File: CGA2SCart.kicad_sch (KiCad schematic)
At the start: 34 parts, among them J1 SCART-F, J2 DB9_Male, J3 Audio-Jack-3_2Switches, J4 DB15_Female_HighDensity, Q1 2N7000

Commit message: Other connections fixed
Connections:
- net at J1.11 (P11), R16.2, R7.2: now also JP3.2 (B), JP7.2 (B)
- net at J1.7 (P7), R17.2, R6.2: now also JP2.2 (B), JP5.2 (B)
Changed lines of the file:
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@@
   (junction (at 221.615 96.52) (diameter 0) (color 0 0 0 0)
   )
+  (junction (at 151.13 97.79) (diameter 0) (color 0 0 0 0)
+  )
   (junction (at 142.875 102.87) (diameter 0) (color 0 0 0 0)
   )
@@
   (junction (at 165.735 87.63) (diameter 0) (color 0 0 0 0)
   )
+  (junction (at 156.845 87.63) (diameter 0) (color 0 0 0 0)
+  )
   (junction (at 151.13 131.445) (diameter 0) (color 0 0 0 0)
   )
@@
     (stroke (width 0) (type default) (color 0 0 0 0))
   )
+  (wire (pts (xy 156.845 87.63) (xy 165.735 87.63))
+    (stroke (width 0) (type default) (color 0 0 0 0))
+  )
   (wire (pts (xy 156.845 131.445) (xy 162.56 131.445))
     (stroke (width 0) (type default) (color 0 0 0 0))
@@
     (stroke (width 0) (type default) (color 0 0 0 0))
   )
-  (wire (pts (xy 156.845 74.295) (xy 156.845 102.235))
+  (wire (pts (xy 151.13 97.79) (xy 165.735 97.79))
     (stroke (width 0) (type default) (color 0 0 0 0))
   )
@@
     (stroke (width 0) (type default) (color 0 0 0 0))
   )
-  (wire (pts (xy 140.97 87.63) (xy 165.735 87.63))
+  (wire (pts (xy 140.97 87.63) (xy 156.845 87.63))
     (stroke (width 0) (type default) (color 0 0 0 0))
   )
@@
     (stroke (width 0) (type default) (color 0 0 0 0))
   )
+  (wire (pts (xy 156.845 87.63) (xy 156.845 102.235))
+    (stroke (width 0) (type default) (color 0 0 0 0))
+  )
   (wire (pts (xy 221.615 135.89) (xy 224.155 135.89))
     (stroke (width 0) (type default) (color 0 0 0 0))
   )
-  (wire (pts (xy 140.97 97.79) (xy 165.735 97.79))
+  (wire (pts (xy 140.97 97.79) (xy 151.13 97.79))
     (stroke (width 0) (type default) (color 0 0 0 0))
   )
@@
     (stroke (width 0) (type default) (color 0 0 0 0))
   )
+  (wire (pts (xy 156.845 74.295) (xy 156.845 87.63))
+    (stroke (width 0) (type default) (color 0 0 0 0))
+  )
   (wire (pts (xy 95.25 104.775) (xy 99.695 104.775))
     (stroke (width 0) (type default) (color 0 0 0 0))
@@
     (stroke (width 0) (type default) (color 0 0 0 0))
   )
+  (wire (pts (xy 151.13 97.79) (xy 151.13 102.235))
+    (stroke (width 0) (type default) (color 0 0 0 0))
+  )
+  (wire (pts (xy 151.13 74.295) (xy 151.13 97.79))
+    (stroke (width 0) (type default) (color 0 0 0 0))
+  )
   (wire (pts (xy 162.56 130.175) (xy 162.56 131.445))
     (stroke (width 0) (type default) (color 0 0 0 0))
@@
     (stroke (width 0) (type default) (color 0 0 0 0))
   )
-  (wire (pts (xy 151.13 74.295) (xy 151.13 102.235))
-    (stroke (width 0) (type default) (color 0 0 0 0))
-  )

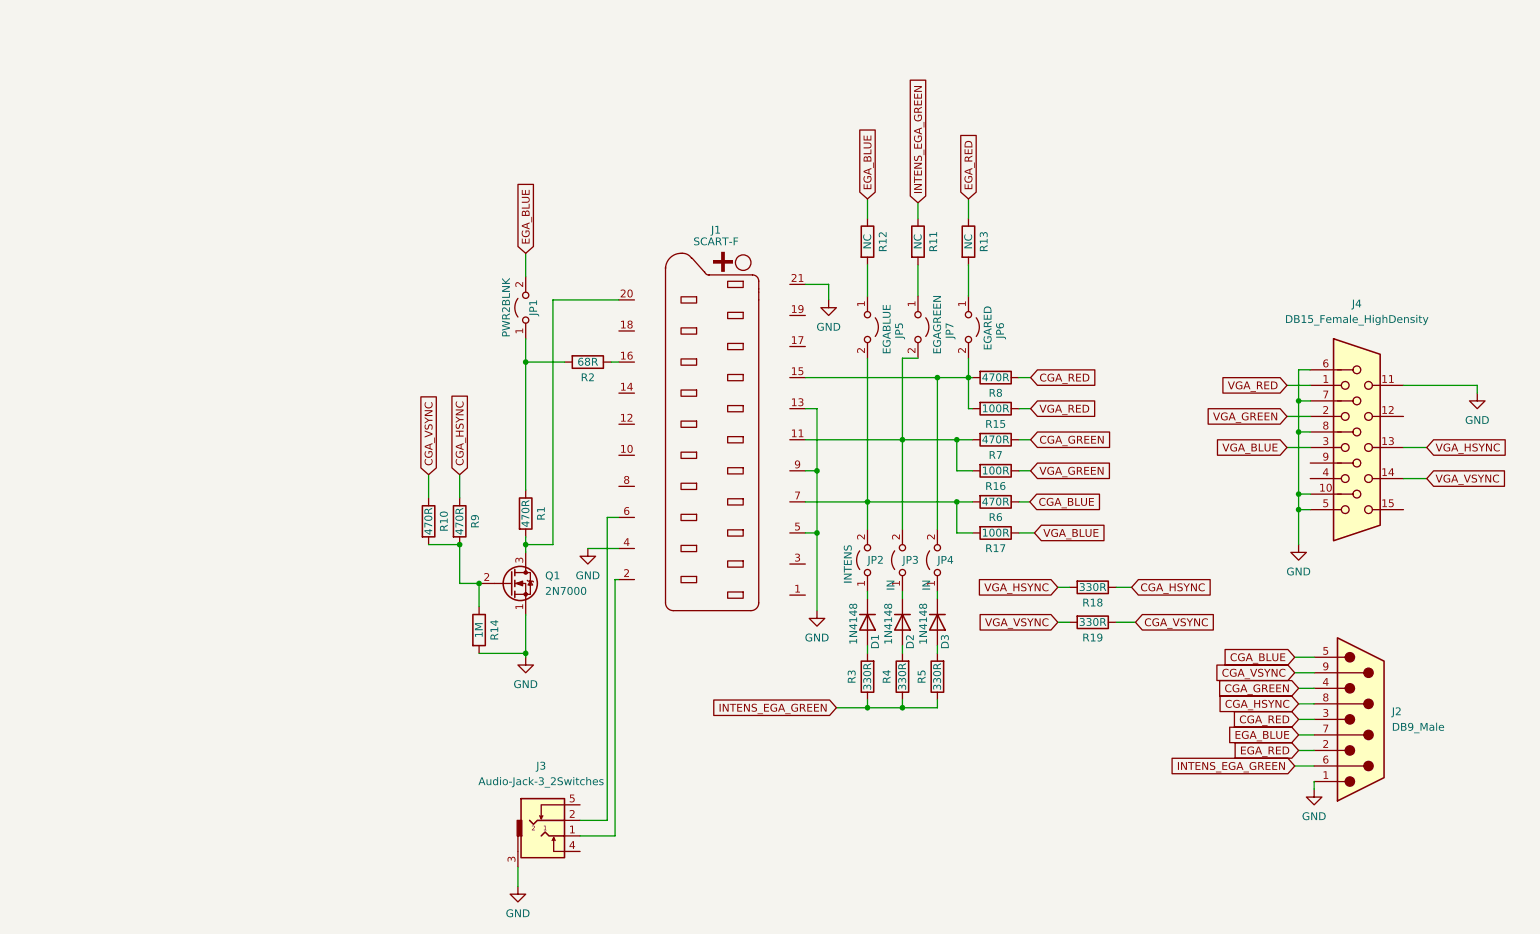
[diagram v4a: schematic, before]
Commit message: V3 of CGA2SCART, change CSYNC to XOR presync
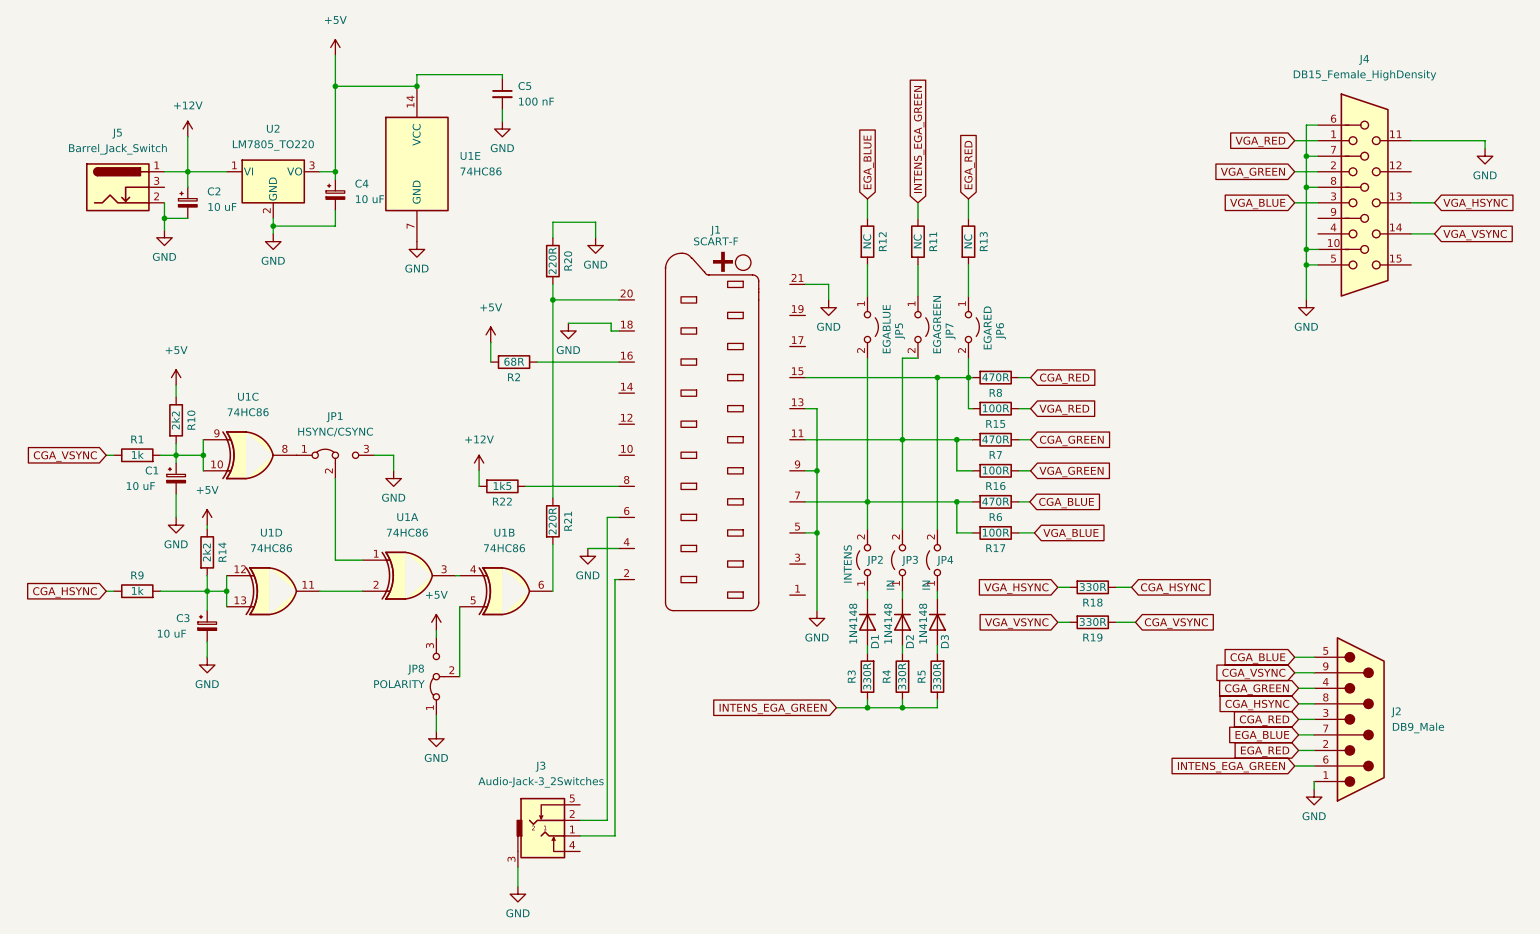
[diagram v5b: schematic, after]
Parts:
- removed JP1: PWR2BLNK, Connector_PinHeader_2.54mm:PinHeader_1x02_P2.54mm_Vertical, symbol Jumper:Jumper_2_Open
- removed Q1: 2N7000, Package_TO_SOT_THT:TO-92_Inline_Wide, symbol Transistor_FET:2N7000
- added C1, C2, C3, C4: 10 uF, Capacitor_THT:CP_Radial_D5.0mm_P2.00mm, symbol Device:C_Polarized_Small
- added C5: 100 nF, Capacitor_THT:C_Disc_D5.0mm_W2.5mm_P5.00mm, symbol Device:C_Small
- added J5: Barrel_Jack_Switch, Connector_BarrelJack:BarrelJack_Horizontal, symbol Connector:Barrel_Jack_Switch
- added JP1: HSYNC/CSYNC, Connector_PinHeader_2.54mm:PinHeader_1x03_P2.54mm_Vertical, symbol Jumper:Jumper_3_Bridged12
- added JP8: POLARITY, Connector_PinHeader_2.54mm:PinHeader_1x03_P2.54mm_Vertical, symbol Jumper:Jumper_3_Bridged12
- added R20, R21: 220R, Resistor_THT:R_Axial_DIN0207_L6.3mm_D2.5mm_P7.62mm_Horizontal, symbol Device:R
- added R22: 1k5, Resistor_THT:R_Axial_DIN0207_L6.3mm_D2.5mm_P7.62mm_Horizontal, symbol Device:R
- added U1: 74HC86, Package_DIP:DIP-14_W7.62mm_Socket, symbol 74xx:74HC86
- added U2: LM7805_TO220, Package_TO_SOT_THT:TO-220-3_Vertical, symbol Regulator_Linear:LM7805_TO220
- R1, R9: value 470R -> 1k
- R10: value 470R -> 2k2
- R14: value 1M -> 2k2
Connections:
- net CGA_VSYNC: now also R1.1; no longer R10.1
- net GND: now also J1.18 (P18), C1.2, C2.2, C3.2, C4.2, C5.2, J5.2, JP1.3 (B), JP8.1 (A), R20.1, U1.7 (GND), U2.2 (GND); no longer R14.2
- net at J1.20 (P20): now also R20.2, R21.1; no longer R1.2
- net at J1.8 (P8): now also R22.1
- net +5V: now reaches R2.2
- net +5V: now also R10.1, R14.1, C4.1, C5.1, JP8.3 (B), U1.14 (VCC), U2.3 (VO); no longer R1.1
- new net: C1.1, R1.2, R10.2, U1.10, U1.9
- new net: JP1.1 (A), U1.8
- new net: JP1.2 (C), U1.1
- new net: U1.3, U1.4
- new net: JP8.2 (C), U1.5
- new net: R21.2, U1.6
- new net: C3.1, R14.2, R9.2, U1.12, U1.13
- new net: U1.11, U1.2
- new net +12V: C2.1, J5.1, R22.2, U2.1 (VI)
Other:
- moved on the sheet: J4, R2

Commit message: Fixed stupid double XOR thing, why can't I get this right?
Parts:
- removed R10, R14: 2k2, Resistor_THT:R_Axial_DIN0207_L6.3mm_D2.5mm_P7.62mm_Horizontal, symbol Device:R
- C1, C3: value 10 uF -> 1 uF
- R1, R9: value 1k -> 10k
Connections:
- net CGA_HSYNC: now also U1.13
- net CGA_VSYNC: now also U1.10
- net at C1.1, R1.2, U1.9: no longer U1.10
- net at C3.1, R9.2, U1.12: no longer U1.13

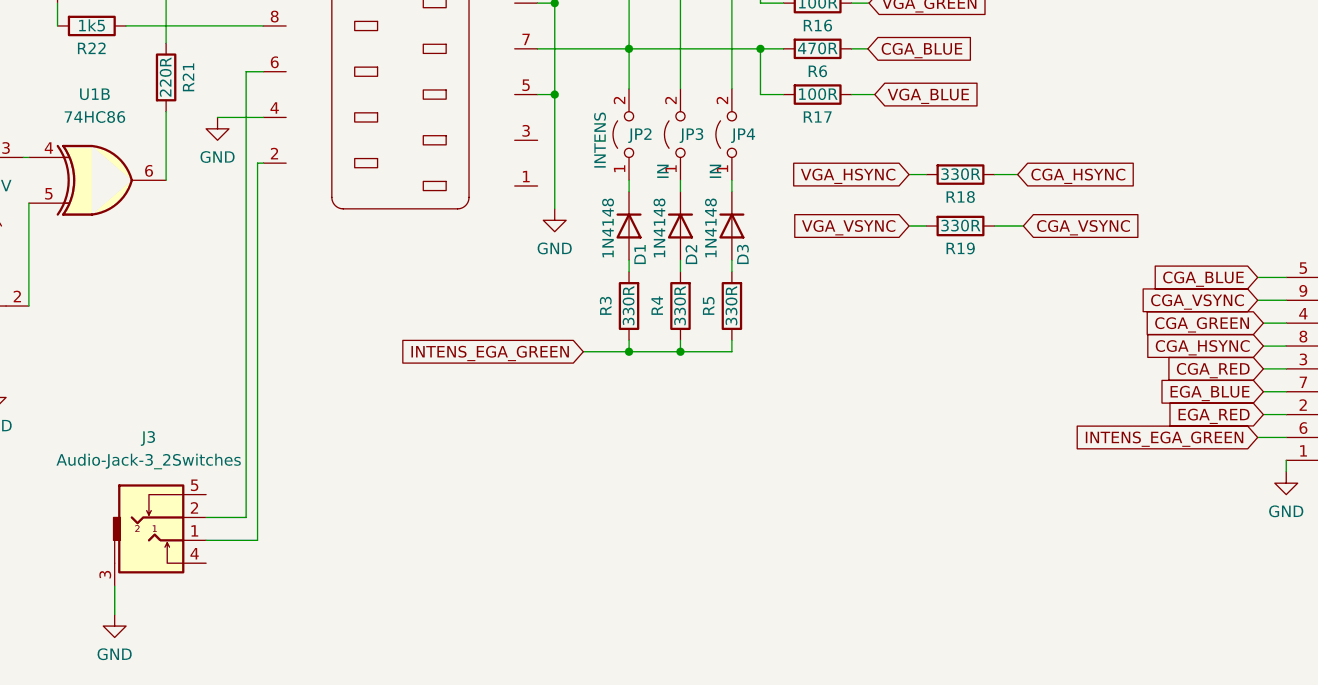
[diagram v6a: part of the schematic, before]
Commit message: Added CSYNC to VGA option
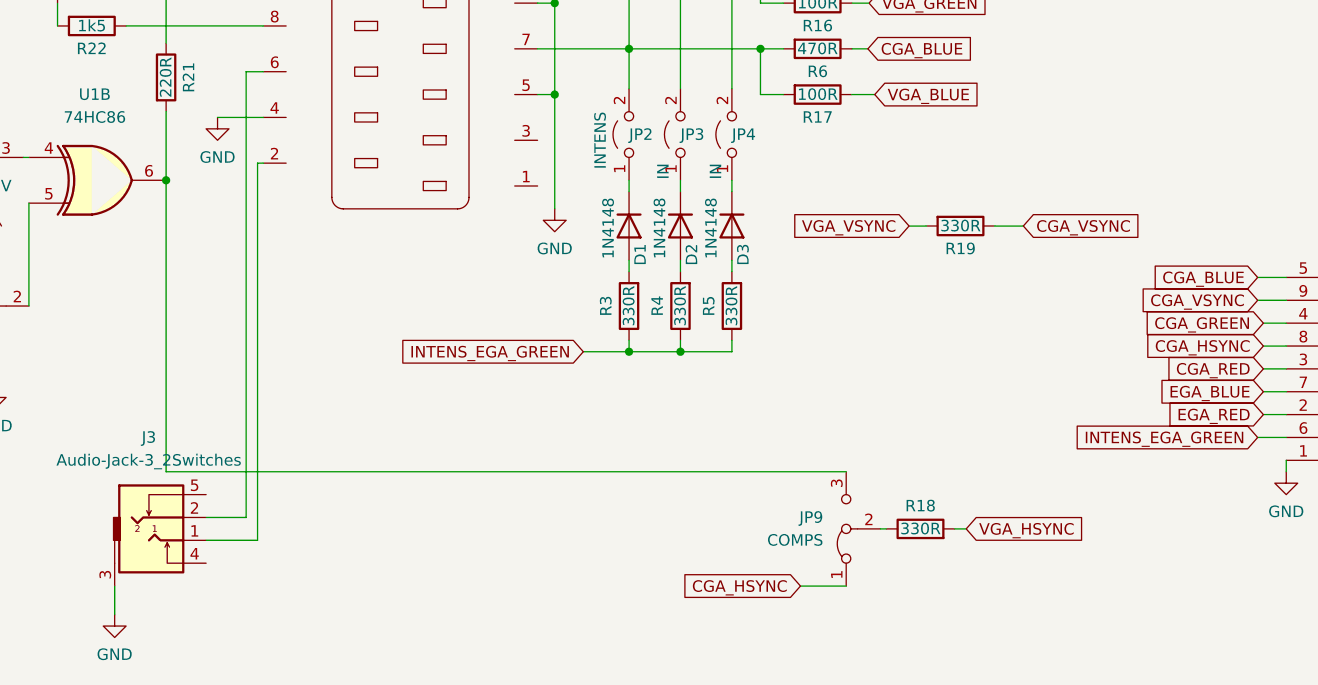
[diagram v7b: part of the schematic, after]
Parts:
- added JP9: COMPS, Connector_PinHeader_2.54mm:PinHeader_1x03_P2.54mm_Vertical, symbol Jumper:Jumper_3_Bridged12
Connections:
- net CGA_HSYNC: now also JP9.1 (A); no longer R18.1
- net at R21.2, U1.6: now also JP9.3 (B)
- new net: JP9.2 (C), R18.1
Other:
- moved on the sheet: R18
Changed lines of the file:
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@@
   (junction (at 36.195 51.435) (diameter 0) (color 0 0 0 0)
   )
+  (junction (at 99.695 112.395) (diameter 0) (color 0 0 0 0)
+  )
   (junction (at 156.845 131.445) (diameter 0) (color 0 0 0 0)
   )
@@
     (stroke (width 0) (type default) (color 0 0 0 0))
   )
+  (wire (pts (xy 170.18 157.48) (xy 175.26 157.48))
+    (stroke (width 0) (type default) (color 0 0 0 0))
+  )
   (wire (pts (xy 175.895 82.55) (xy 177.8 82.55))
     (stroke (width 0) (type default) (color 0 0 0 0))
@@
     (stroke (width 0) (type default) (color 0 0 0 0))
   )
+  (wire (pts (xy 99.695 144.78) (xy 175.26 144.78))
+    (stroke (width 0) (type default) (color 0 0 0 0))
+  )
   (wire (pts (xy 105.41 105.41) (xy 110.49 105.41))
     (stroke (width 0) (type default) (color 0 0 0 0))
@@
     (stroke (width 0) (type default) (color 0 0 0 0))
   )
+  (wire (pts (xy 187.325 151.13) (xy 188.595 151.13))
+    (stroke (width 0) (type default) (color 0 0 0 0))
+  )
   (wire (pts (xy 191.77 117.475) (xy 194.945 117.475))
     (stroke (width 0) (type default) (color 0 0 0 0))
@@
     (stroke (width 0) (type default) (color 0 0 0 0))
   )
+  (wire (pts (xy 179.07 151.13) (xy 179.705 151.13))
+    (stroke (width 0) (type default) (color 0 0 0 0))
+  )
   (wire (pts (xy 40.005 43.815) (xy 46.355 43.815))
     (stroke (width 0) (type default) (color 0 0 0 0))
@@
     (stroke (width 0) (type default) (color 0 0 0 0))
   )
-  (wire (pts (xy 182.245 111.76) (xy 184.15 111.76))
-    (stroke (width 0) (type default) (color 0 0 0 0))
-  )
   (wire (pts (xy 26.67 90.17) (xy 27.305 90.17))
     (stroke (width 0) (type default) (color 0 0 0 0))
@@
     (stroke (width 0) (type default) (color 0 0 0 0))
   )
+  (wire (pts (xy 99.695 112.395) (xy 99.695 144.78))
+    (stroke (width 0) (type default) (color 0 0 0 0))
+  )
   (wire (pts (xy 53.975 52.705) (xy 53.975 53.975))
     (stroke (width 0) (type default) (color 0 0 0 0))
@@
   )
   (wire (pts (xy 156.845 121.285) (xy 156.845 122.555))
-    (stroke (width 0) (type default) (color 0 0 0 0))
-  )
-  (wire (pts (xy 191.77 111.76) (xy 194.31 111.76))
     (stroke (width 0) (type default) (color 0 0 0 0))
   )
@@
     )
   )
-  (global_label "VGA_HSYNC" (shape input) (at 182.245 111.76 180) (fields_autoplaced)
-    (effects (font (size 1.27 1.27)) (justify right))
-    (property "Intersheet References" "${INTERSHEET_REFS}" (id 0) (at 169.1881 111.8394 0)
-      (effects (font (size 1.27 1.27)) (justify right) hide)
+  (global_label "VGA_HSYNC" (shape input) (at 188.595 151.13 0) (fields_autoplaced)
+    (effects (font (size 1.27 1.27)) (justify left))
+    (property "Intersheet References" "${INTERSHEET_REFS}" (id 0) (at 201.6519 151.0506 0)
+      (effects (font (size 1.27 1.27)) (justify left) hide)
     )
   )
@@
     )
   )
-  (global_label "CGA_HSYNC" (shape input) (at 194.31 111.76 0) (fields_autoplaced)
-    (effects (font (size 1.27 1.27)) (justify left))
-    (property "Intersheet References" "${INTERSHEET_REFS}" (id 0) (at 207.5483 111.8394 0)
-      (effects (font (size 1.27 1.27)) (justify left) hide)
+  (global_label "CGA_HSYNC" (shape input) (at 170.18 157.48 180) (fields_autoplaced)
+    (effects (font (size 1.27 1.27)) (justify right))
+    (property "Intersheet References" "${INTERSHEET_REFS}" (id 0) (at 156.9417 157.4006 0)
+      (effects (font (size 1.27 1.27)) (justify right) hide)
     )
   )
@@
     (pin "1")
   )
-  (symbol (lib_id "Device:R") (at 187.96 111.76 270) (unit 1)
-    (in_bom yes) (on_board yes)
-    (property "Reference" "R18" (id 0) (at 187.96 114.3 90))
-    (property "Value" "330R" (id 1) (at 187.96 111.76 90))
-    (property "Footprint" "Resistor_THT:R_Axial_DIN0207_L6.3mm_D2.5mm_P7.62mm_Horizontal" (id 2) (at 187.96 109.982 90)
-      (effects (font (size 1.27 1.27)) hide)
-    )
-    (property "Datasheet" "~" (id 3) (at 187.96 111.76 0)
+  (symbol (lib_id "Device:R") (at 183.515 151.13 90) (unit 1)
+    (in_bom yes) (on_board yes)
+    (property "Reference" "R18" (id 0) (at 183.515 148.59 90))
+    (property "Value" "330R" (id 1) (at 183.515 151.13 90))
+    (property "Footprint" "Resistor_THT:R_Axial_DIN0207_L6.3mm_D2.5mm_P7.62mm_Horizontal" (id 2) (at 183.515 152.908 90)
+      (effects (font (size 1.27 1.27)) hide)
+    )
+    (property "Datasheet" "~" (id 3) (at 183.515 151.13 0)
       (effects (font (size 1.27 1.27)) hide)
     )
@@
     (pin "2")
   )
+  (symbol (lib_id "Jumper:Jumper_3_Bridged12") (at 175.26 151.13 90) (unit 1)
+    (in_bom yes) (on_board yes) (fields_autoplaced)
+    (property "Reference" "JP9" (id 0) (at 172.72 149.8599 90)
+      (effects (font (size 1.27 1.27)) (justify left))
+    )
+    (property "Value" "COMPS" (id 1) (at 172.72 152.3999 90)
+      (effects (font (size 1.27 1.27)) (justify left))
+    )
+    (property "Footprint" "Connector_PinHeader_2.54mm:PinHeader_1x03_P2.54mm_Vertical" (id 2) (at 175.26 151.13 0)
+      (effects (font (size 1.27 1.27)) hide)
+    )
+    (property "Datasheet" "~" (id 3) (at 175.26 151.13 0)
+      (effects (font (size 1.27 1.27)) hide)
+    )
+    (pin "1")
+    (pin "2")
+    (pin "3")
+  )
   (symbol (lib_id "Device:R") (at 172.085 87.63 270) (unit 1)
     (in_bom yes) (on_board yes)
@@
       (reference "JP8") (unit 1) (value "POLARITY") (footprint "Connector_PinHeader_2.54mm:PinHeader_1x03_P2.54mm_Vertical")
     )
+    (path "/8f03ae41-61bd-4463-bc12-db0dde34447c"
+      (reference "JP9") (unit 1) (value "COMPS") (footprint "Connector_PinHeader_2.54mm:PinHeader_1x03_P2.54mm_Vertical")
+    )
     (path "/dea26430-4380-44d1-9394-b9619f5a7ab8"
